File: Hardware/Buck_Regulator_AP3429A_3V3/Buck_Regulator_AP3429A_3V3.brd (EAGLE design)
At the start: 25.4 x 25.4 mm, 53 parts, among them J1 Screw Terminal, J2 POWER_JACKPOWER_JACK_SLOT_COM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, J3 Breakout Headers, U1 AP3429/A

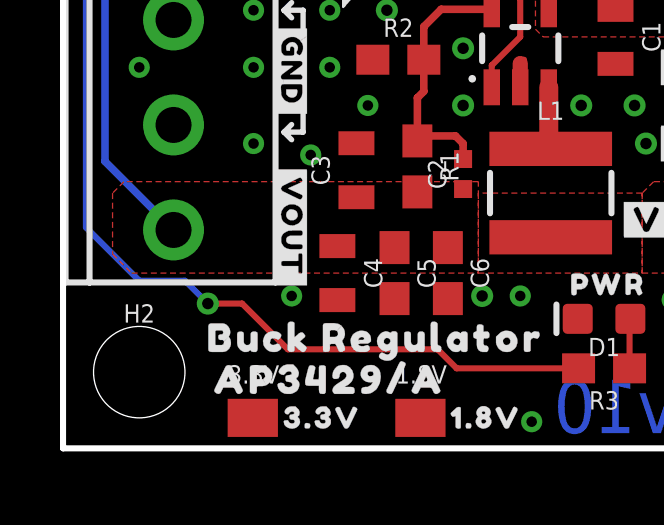
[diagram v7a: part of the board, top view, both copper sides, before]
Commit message: Design Review changes
Cleaned up 1.8V Hardware folder by deleting unneeded files, adjusted schematic notes for easier reading, deleted extraneous measures, adjusted GND via sizes to be the same size (15mil), adjusted some vias for better GND plane connection
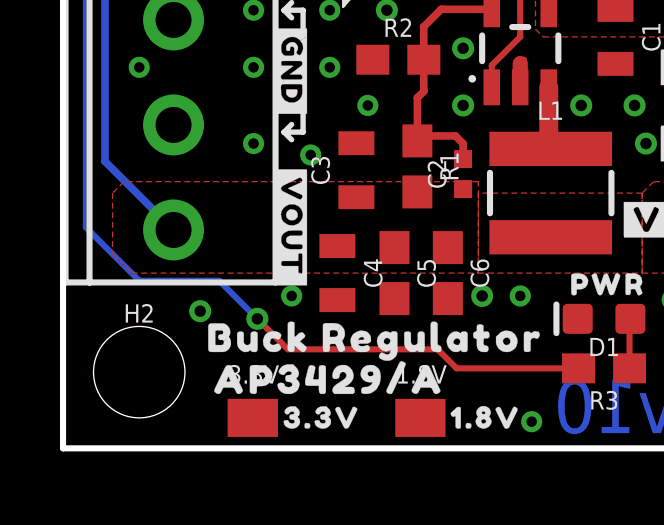
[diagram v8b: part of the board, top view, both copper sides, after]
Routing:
- net GND: vias 30 -> 31
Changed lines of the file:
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@@
 <drawing>
 <settings>
-<setting alwaysvectorfont="yes"/>
+<setting alwaysvectorfont="no"/>
 <setting verticaltext="up"/>
 </settings>
@@
 <layer number="45" name="Holes" color="7" fill="1" visible="yes" active="yes"/>
 <layer number="46" name="Milling" color="3" fill="1" visible="no" active="yes"/>
-<layer number="47" name="Measures" color="7" fill="1" visible="no" active="yes"/>
+<layer number="47" name="Measures" color="7" fill="1" visible="yes" active="yes"/>
 <layer number="48" name="Document" color="7" fill="1" visible="no" active="yes"/>
 <layer number="49" name="Reference" color="7" fill="1" visible="no" active="yes"/>
@@
 <dimension x1="3.683" y1="7.28" x2="3.81" y2="0" x3="-1.651" y3="3.64" textsize="1.778" textratio="15" layer="47" dtype="vertical" unit="inch"/>
 <dimension x1="24.13" y1="7.62" x2="24.13" y2="0" x3="-5.334" y3="3.81" textsize="1.778" textratio="15" layer="47" dtype="vertical" unit="inch"/>
-<dimension x1="25.4" y1="0" x2="24.13" y2="10.16" x3="-9.271" y3="5.08" textsize="1.778" textratio="15" layer="47" dtype="vertical" unit="inch"/>
-<dimension x1="3.683" y1="10.795" x2="3.683" y2="0" x3="-12.827" y3="5.3975" textsize="1.778" textratio="15" layer="47" dtype="vertical" unit="inch"/>
 <text x="-25.4" y="-12.7" size="1.778" layer="47" font="vector" ratio="15">Units in Inches</text>
 <wire x1="3.048" y1="16.891" x2="3.048" y2="6.35" width="5.9944" layer="48"/>
 <wire x1="3.048" y1="6.35" x2="0" y2="3.302" width="5.9944" layer="48"/>
-<dimension x1="6.35" y1="3.81" x2="0" y2="3.81" x3="3.175" y3="-11.43" textsize="1.778" textratio="15" layer="47" unit="inch"/>
-<dimension x1="13.335" y1="24.003" x2="0" y2="24.003" x3="6.6675" y3="-16.51" textsize="1.778" textratio="15" layer="47" unit="inch"/>
-<dimension x1="22.86" y1="2.54" x2="0" y2="2.54" x3="11.43" y3="-21.59" textsize="1.778" textratio="15" layer="47" unit="inch"/>
-<dimension x1="24.13" y1="7.62" x2="0" y2="7.62" x3="12.065" y3="-25.4" textsize="1.778" textratio="15" layer="47" unit="inch"/>
-<dimension x1="25.4" y1="0" x2="0" y2="0" x3="12.7" y3="-29.21" textsize="1.778" textratio="15" layer="47" unit="inch"/>
-<dimension x1="6.35" y1="3.81" x2="6.35" y2="0" x3="-16.51" y3="1.905" textsize="1.778" textratio="15" layer="47" unit="inch"/>
-<dimension x1="2.54" y1="2.54" x2="2.54" y2="0" x3="-20.32" y3="1.27" textsize="1.778" textratio="15" layer="47" unit="inch"/>
-<dimension x1="2.54" y1="22.86" x2="2.54" y2="0" x3="-24.13" y3="11.43" textsize="1.778" textratio="15" layer="47" unit="inch"/>
-<dimension x1="13.335" y1="24.003" x2="13.335" y2="0" x3="-27.94" y3="12.0015" textsize="1.778" textratio="15" layer="47" unit="inch"/>
-<dimension x1="0" y1="0" x2="0" y2="25.4" x3="-31.75" y3="12.7" textsize="1.778" textratio="15" layer="47" unit="inch"/>
-<dimension x1="21.59" y1="3.81" x2="21.59" y2="16.51" x3="30.48" y3="10.16" textsize="1.778" textratio="15" layer="47" unit="inch"/>
-<dimension x1="6.35" y1="16.51" x2="21.59" y2="16.51" x3="13.97" y3="35.56" textsize="1.778" textratio="15" layer="47" unit="inch"/>
+<dimension x1="13.335" y1="24.003" x2="0" y2="24.003" x3="6.6675" y3="-12.7" textsize="1.778" textratio="15" layer="47" unit="inch"/>
+<dimension x1="22.86" y1="2.54" x2="0" y2="2.54" x3="11.43" y3="-17.78" textsize="1.778" textratio="15" layer="47" unit="inch"/>
+<dimension x1="24.13" y1="7.62" x2="0" y2="7.62" x3="12.065" y3="-21.59" textsize="1.778" textratio="15" layer="47" unit="inch"/>
+<dimension x1="25.4" y1="0" x2="0" y2="0" x3="12.7" y3="-25.4" textsize="1.778" textratio="15" layer="47" unit="inch"/>
+<dimension x1="2.54" y1="2.54" x2="2.54" y2="0" x3="-10.16" y3="1.27" textsize="1.778" textratio="15" layer="47" unit="inch"/>
+<dimension x1="2.54" y1="22.86" x2="2.54" y2="0" x3="-13.97" y3="11.43" textsize="1.778" textratio="15" layer="47" unit="inch"/>
+<dimension x1="13.335" y1="24.003" x2="13.335" y2="0" x3="-17.78" y3="12.0015" textsize="1.778" textratio="15" layer="47" unit="inch"/>
+<dimension x1="0" y1="25.4" x2="0" y2="0" x3="-21.59" y3="12.7" textsize="1.778" textratio="15" layer="47" unit="inch"/>
 </plain>
 <attributes>
@@
 <contactref element="C6" pad="2"/>
 <via x="13.97" y="5.08" extent="1-16" drill="0.381"/>
+<via x="4.572" y="4.572" extent="1-16" drill="0.381"/>
 </signal>
 <signal name="N$1">
@@
 <wire x1="12.485" y1="3.302" x2="13.12" y2="2.667" width="0.2032" layer="1"/>
 <wire x1="12.485" y1="3.302" x2="7.493" y2="3.302" width="0.2032" layer="1"/>
-<via x="4.826" y="4.826" extent="1-16" drill="0.381"/>
-<wire x1="4.826" y1="4.826" x2="5.969" y2="4.826" width="0.2032" layer="1"/>
-<wire x1="5.969" y1="4.826" x2="7.493" y2="3.302" width="0.2032" layer="1"/>
+<via x="6.477" y="4.318" extent="1-16" drill="0.381"/>
+<wire x1="6.477" y1="4.318" x2="7.493" y2="3.302" width="0.2032" layer="1"/>
 <wire x1="0.762" y1="19.431" x2="0.762" y2="7.366" width="0.2032" layer="16"/>
 <wire x1="0.762" y1="7.366" x2="2.54" y2="5.588" width="0.2032" layer="16"/>
-<wire x1="4.064" y1="5.588" x2="4.826" y2="4.826" width="0.2032" layer="16"/>
-<wire x1="4.064" y1="5.588" x2="2.54" y2="5.588" width="0.2032" layer="16"/>
+<wire x1="5.207" y1="5.588" x2="6.477" y2="4.318" width="0.2032" layer="16"/>
+<wire x1="5.207" y1="5.588" x2="2.54" y2="5.588" width="0.2032" layer="16"/>
 <contactref element="R3" pad="2"/>
 <wire x1="13.12" y1="2.667" x2="17.184" y2="2.667" width="0.2032" layer="1"/>
